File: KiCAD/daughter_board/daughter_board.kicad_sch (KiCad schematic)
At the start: 22 parts, among them IC1 QMC5883L, J1 JST, U1 TPS61023DRLR, U2 SN74AHCT1G125DBVR, U3 XIAO-ESP32-C3-SMD, U4 MPU-6050

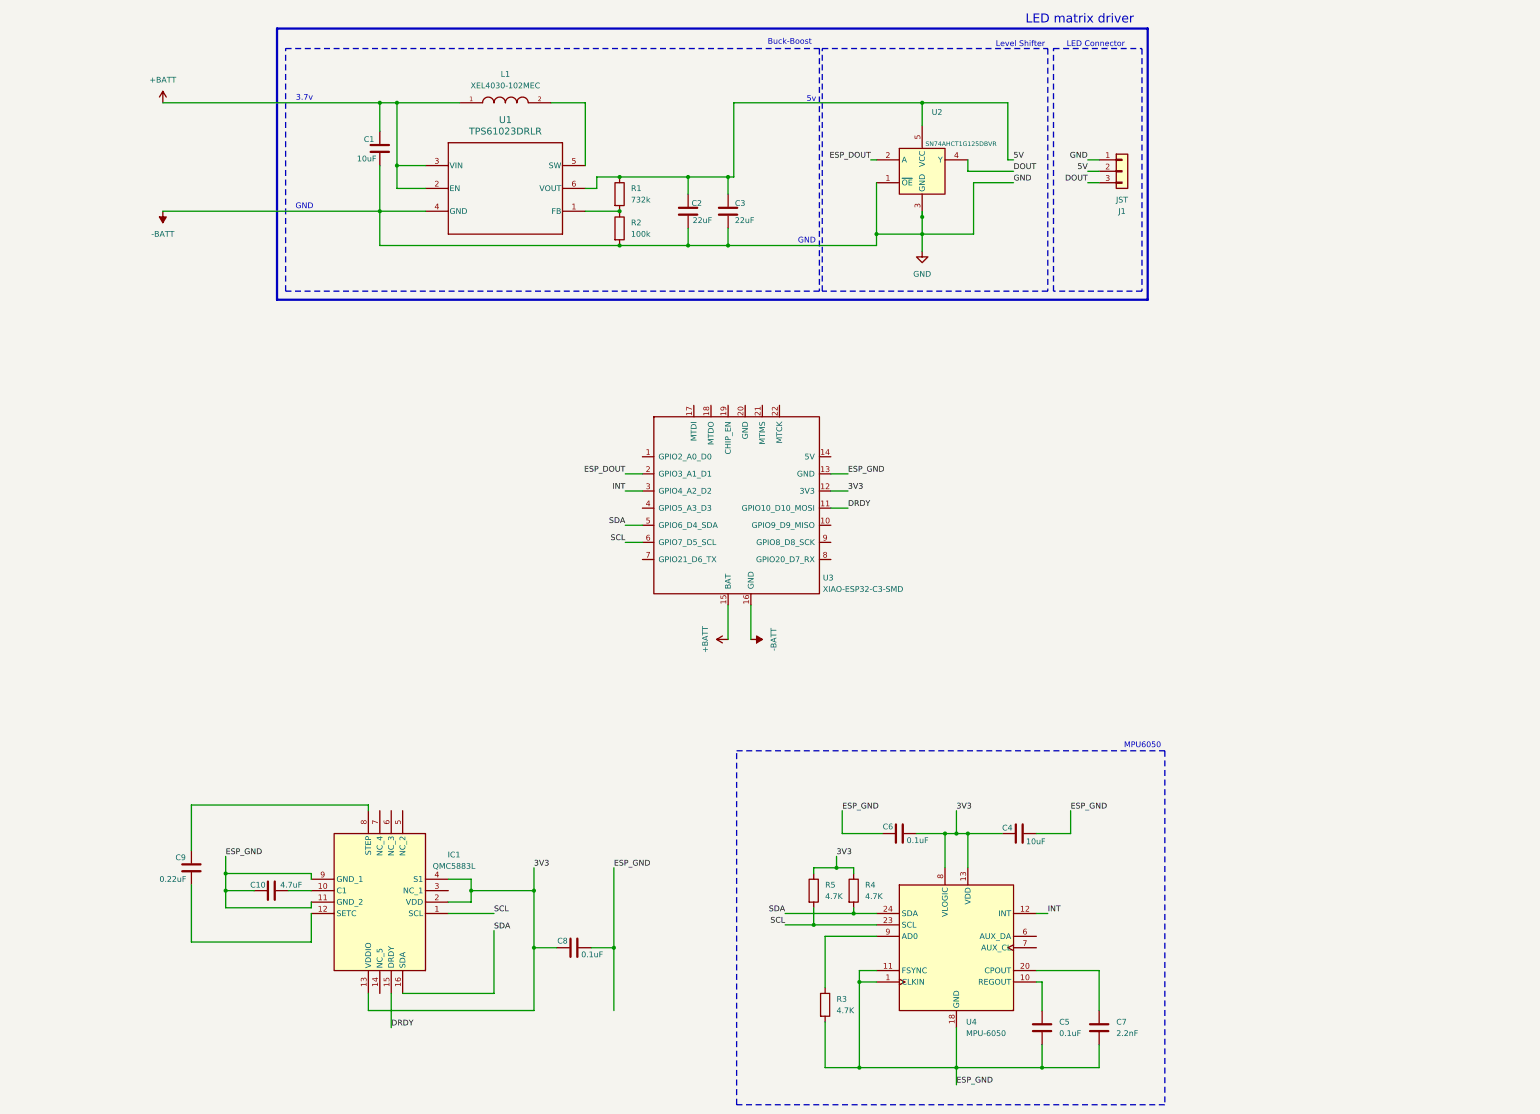
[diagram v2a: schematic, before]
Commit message: kicad schematic finished for the daughter board (initial design)
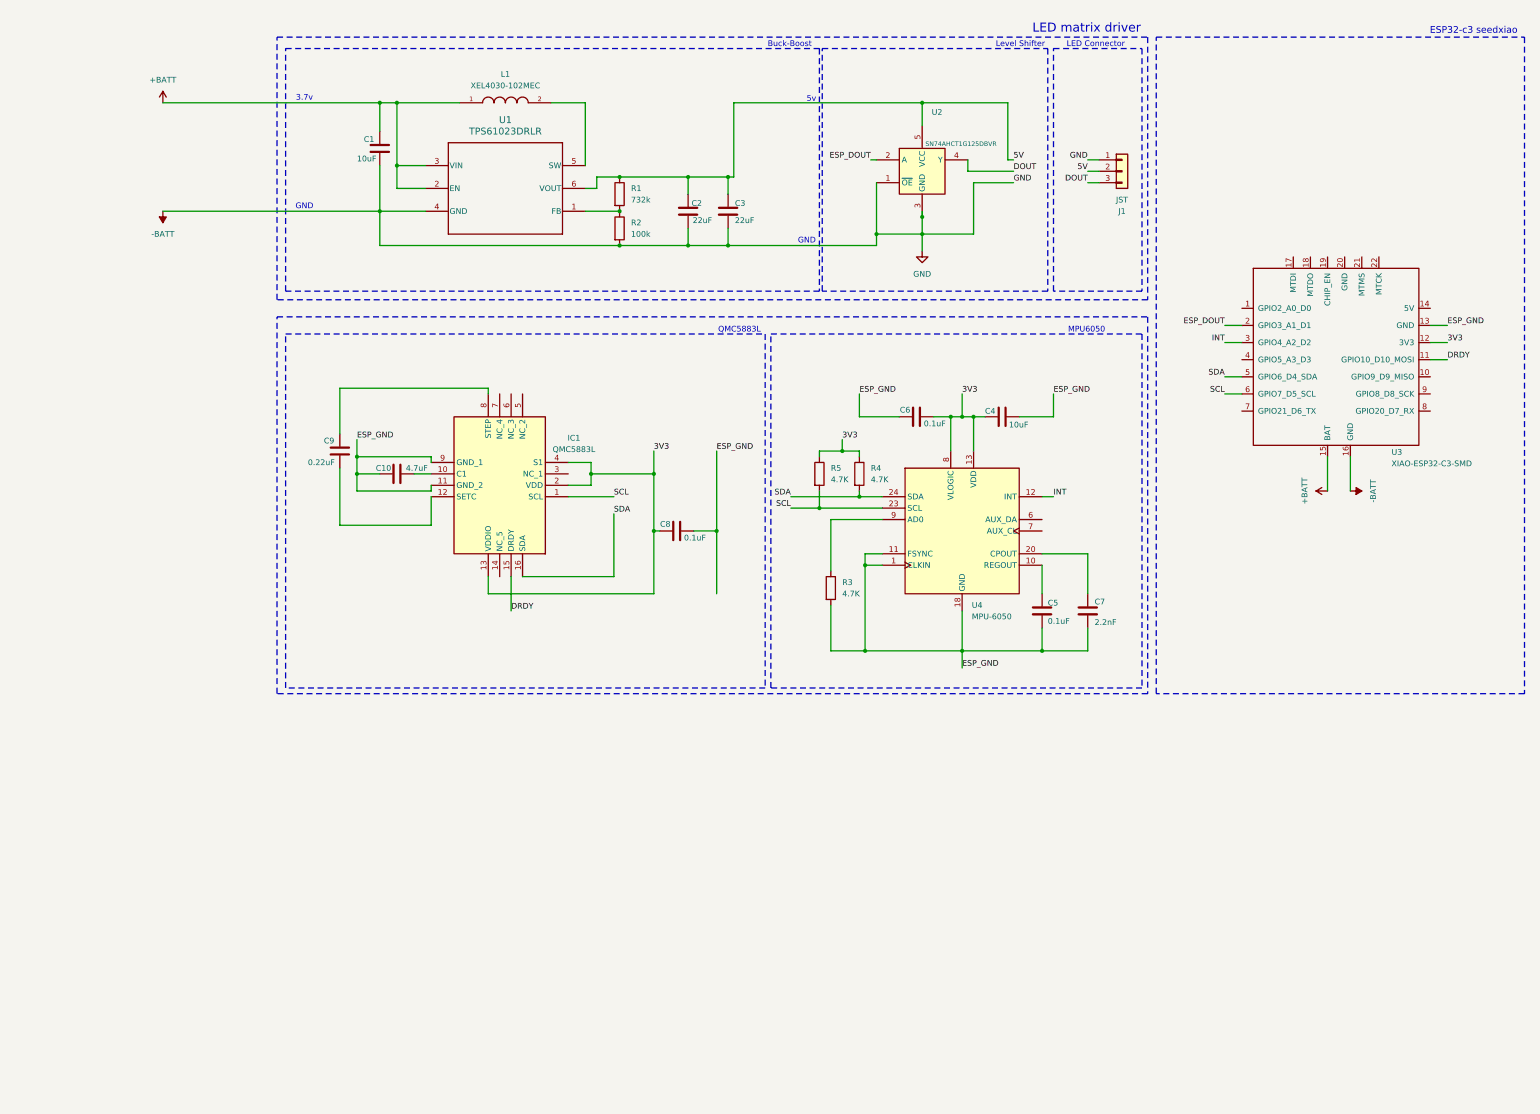
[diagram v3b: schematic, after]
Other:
- note added: "ESP32-c3 seedxiao"
- note added: "QMC5883L"
- moved on the sheet: C10, C4, C5, C6, C7, C8, C9, IC1, R3, R4, R5, U3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

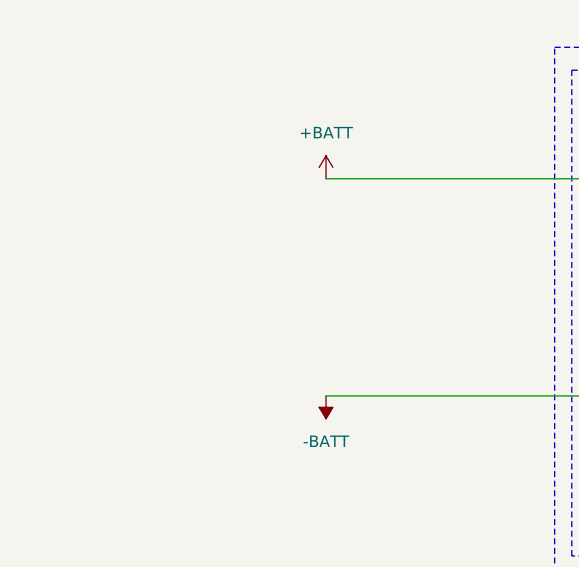
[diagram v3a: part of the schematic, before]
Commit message: added power connector to the schematic, next step is to make the footprint
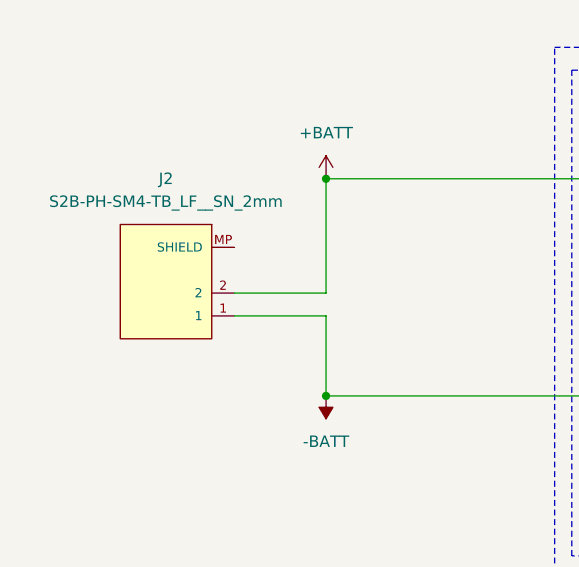
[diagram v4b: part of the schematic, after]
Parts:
- added J2: S2B-PH-SM4-TB_LF__SN_2mm, Connector_JST:JST_PH_S2B-PH-SM4-TB_1x02-1MP_P2.00mm_Horizontal, symbol JST_S2B-PH-SM4-TB_LF__SN_:S2B-PH-SM4-TB_LF__SN_
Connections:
- net +BATT: now also J2.2
- net -BATT: now also J2.1
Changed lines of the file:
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@@
 	)
 	(junction
+		(at 59.69 96.52)
+		(diameter 0)
+		(color 0 0 0 0)
+	)
+	(junction
 		(at 154.94 154.94)
 		(diameter 0)
@@
 	)
 	(junction
+		(at 59.69 72.39)
+		(diameter 0)
+		(color 0 0 0 0)
+	)
+	(junction
 		(at 107.95 72.39)
 		(diameter 0)
@@
 	(wire
 		(pts
+			(xy 49.53 85.09) (xy 59.69 85.09)
+		)
+		(stroke
+			(width 0)
+			(type default)
+		)
+	)
+	(wire
+		(pts
 			(xy 210.82 147.32) (xy 210.82 149.86)
 		)
@@
 	(wire
 		(pts
+			(xy 59.69 85.09) (xy 59.69 72.39)
+		)
+		(stroke
+			(width 0)
+			(type default)
+		)
+	)
+	(wire
+		(pts
 			(xy 240.03 142.24) (xy 240.03 149.86)
 		)
@@
 	(wire
 		(pts
+			(xy 59.69 87.63) (xy 59.69 96.52)
+		)
+		(stroke
+			(width 0)
+			(type default)
+		)
+	)
+	(wire
+		(pts
 			(xy 214.63 142.24) (xy 223.52 142.24)
 		)
@@
 	(wire
 		(pts
+			(xy 49.53 87.63) (xy 59.69 87.63)
+		)
+		(stroke
+			(width 0)
+			(type default)
+		)
+	)
+	(wire
+		(pts
 			(xy 176.53 104.14) (xy 176.53 100.33)
 		)
@@
 					(unit 1)
 				)
+			)
+		)
+	)
+	(symbol
+		(lib_id "JST_S2B-PH-SM4-TB_LF__SN_:S2B-PH-SM4-TB_LF__SN_")
+		(at 41.91 85.09 180)
+		(unit 1)
+		(exclude_from_sim no)
+		(in_bom yes)
+		(on_board yes)
+		(dnp no)
+		(fields_autoplaced yes)
+		(property "Reference" "J2"
+			(at 41.91 72.39 0)
+			(effects
+				(font
+					(size 1.27 1.27)
+				)
+			)
+		)
+		(property "Value" "S2B-PH-SM4-TB_LF__SN_2mm"
+			(at 41.91 74.93 0)
+			(effects
+				(font
+					(size 1.27 1.27)
+				)
+			)
+		)
+		(property "Footprint" "Connector_JST:JST_PH_S2B-PH-SM4-TB_1x02-1MP_P2.00mm_Horizontal"
+			(at 41.91 85.09 0)
+			(effects
+				(font
+					(size 1.27 1.27)
+				)
+				(justify bottom)
+				(hide yes)
+			)
+		)
+		(property "Datasheet" ""
+			(at 41.91 85.09 0)
+			(effects
+				(font
+					(size 1.27 1.27)
+				)
+				(hide yes)
+			)
+		)
+		(property "Description" ""
+			(at 41.91 85.09 0)
+			(effects
+				(font
+					(size 1.27 1.27)
+				)
+				(hide yes)
+			)
+		)
+		(property "MF" "JST Sales"
+			(at 41.91 85.09 0)
+			(effects
+				(font
+					(size 1.27 1.27)
+				)
+				(justify bottom)
+				(hide yes)
+			)
+		)
+		(property "Description_1" "Connector Header Surface Mount, Right Angle 2 position 0.079 (2.00mm)"
+			(at 41.91 85.09 0)
+			(effects
+				(font
+					(size 1.27 1.27)
+				)
+				(justify bottom)
+				(hide yes)
+			)
+		)
+		(property "Package" "None"
+			(at 41.91 85.09 0)
+			(effects
+				(font
+					(size 1.27 1.27)
+				)
+				(justify bottom)
+				(hide yes)
+			)
+		)
+		(property "Price" "None"
+			(at 41.91 85.09 0)
+			(effects
+				(font
+					(size 1.27 1.27)
+				)
+				(justify bottom)
+				(hide yes)
+			)
+		)
+		(property "Check_prices" "https://www.snapeda.com/parts/S2B-PH-SM4-TB(LF)(SN)/JST/view-part/?ref=eda"
+			(at 41.91 85.09 0)
+			(effects
+				(font
+					(size 1.27 1.27)
+				)
+				(justify bottom)
+				(hide yes)
+			)
+		)
+		(property "STANDARD" "Manufacturer Recommendation"
+			(at 41.91 85.09 0)
+			(effects
+				(font
+					(size 1.27 1.27)
+				)
+				(justify bottom)
+				(hide yes)
+			)
+		)
+		(property "SnapEDA_Link" "https://www.snapeda.com/parts/S2B-PH-SM4-TB(LF)(SN)/JST/view-part/?ref=snap"
+			(at 41.91 85.09 0)
+			(effects
+				(font
+					(size 1.27 1.27)
+				)
+				(justify bottom)
+				(hide yes)
+			)
+		)
+		(property "MP" "S2B-PH-SM4-TB(LF)(SN)"
+			(at 41.91 85.09 0)
+			(effects
+				(font
+					(size 1.27 1.27)
+				)
+				(justify bottom)
+				(hide yes)
+			)
+		)
+		(property "Availability" "In Stock"
+			(at 41.91 85.09 0)
+			(effects
+				(font
+					(size 1.27 1.27)
+				)
+				(justify bottom)
+				(hide yes)
+			)
+		)
+		(property "MANUFACTURER" "JST"
+			(at 41.91 85.09 0)
+			(effects
+				(font
+					(size 1.27 1.27)
+				)
+				(justify bottom)
+				(hide yes)
+			)
+		)
+		(pin "1"
+		)
+		(pin "2"
+		)
+		(pin "MP"
+		)
+		(pin "MP"
+		)
+		(instances
+			(project ""
+				(path "/d928dfc7-4203-47ba-85a4-5f555cf64e96"
+					(reference "J2")
+					(unit 1)
+				)

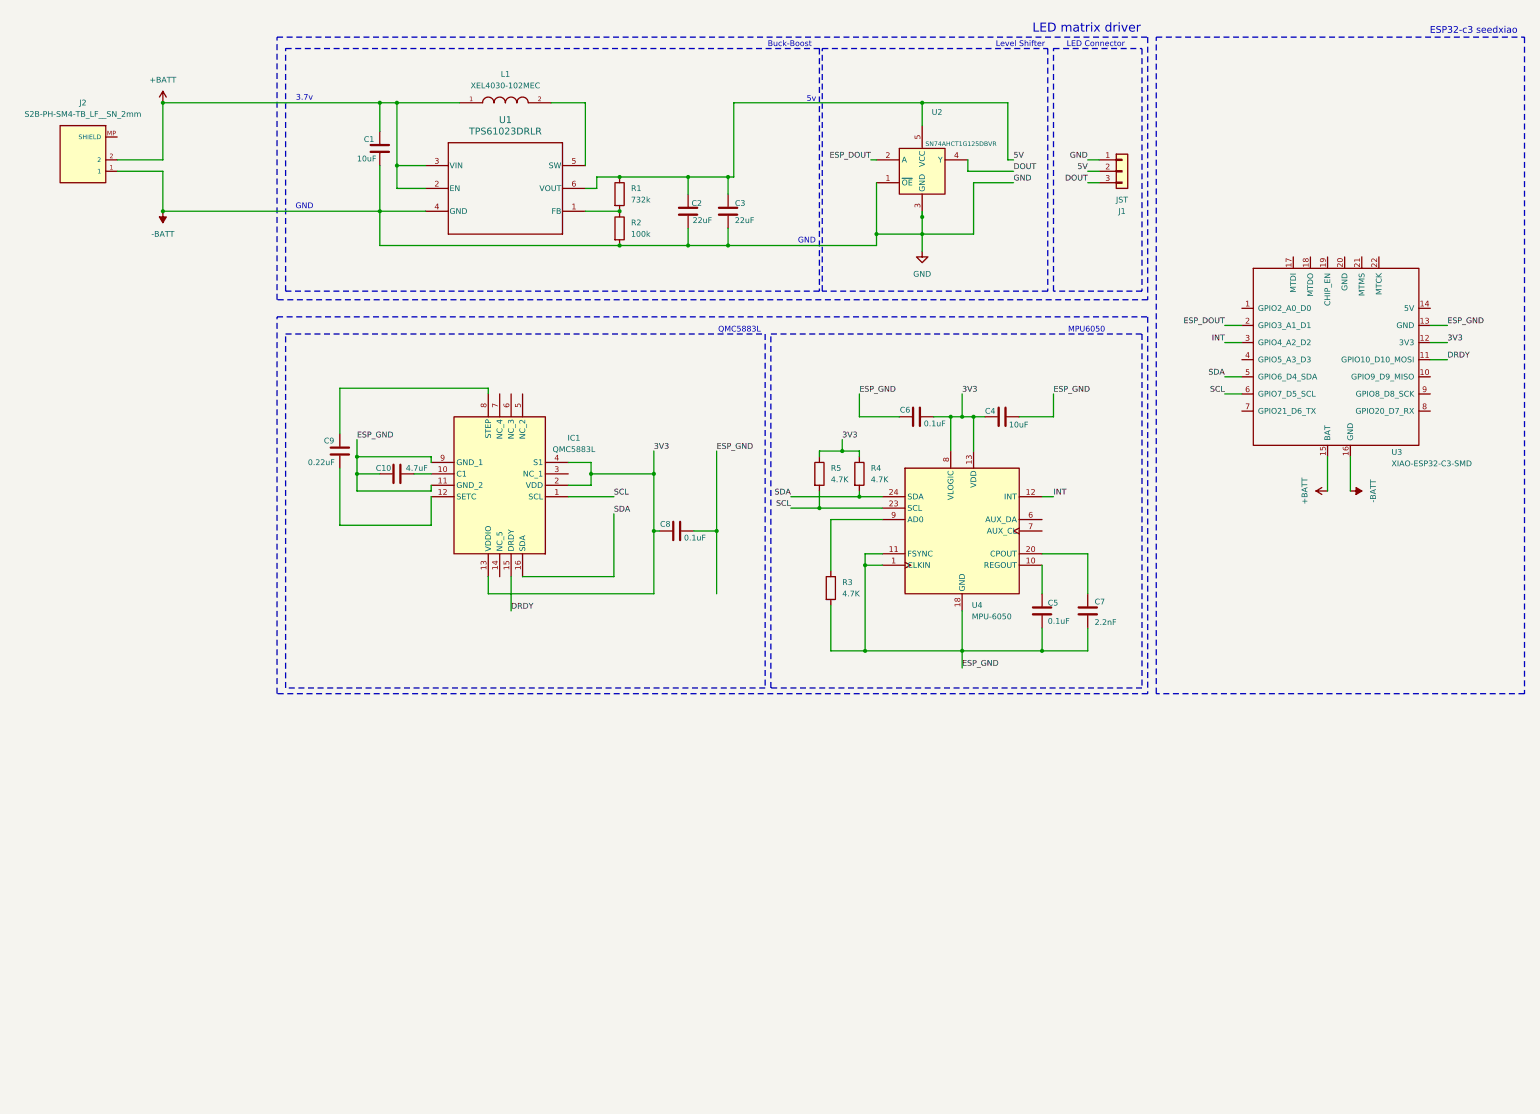
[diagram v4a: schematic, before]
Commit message: completed new freecad base_plate and the KiCAD pcb design
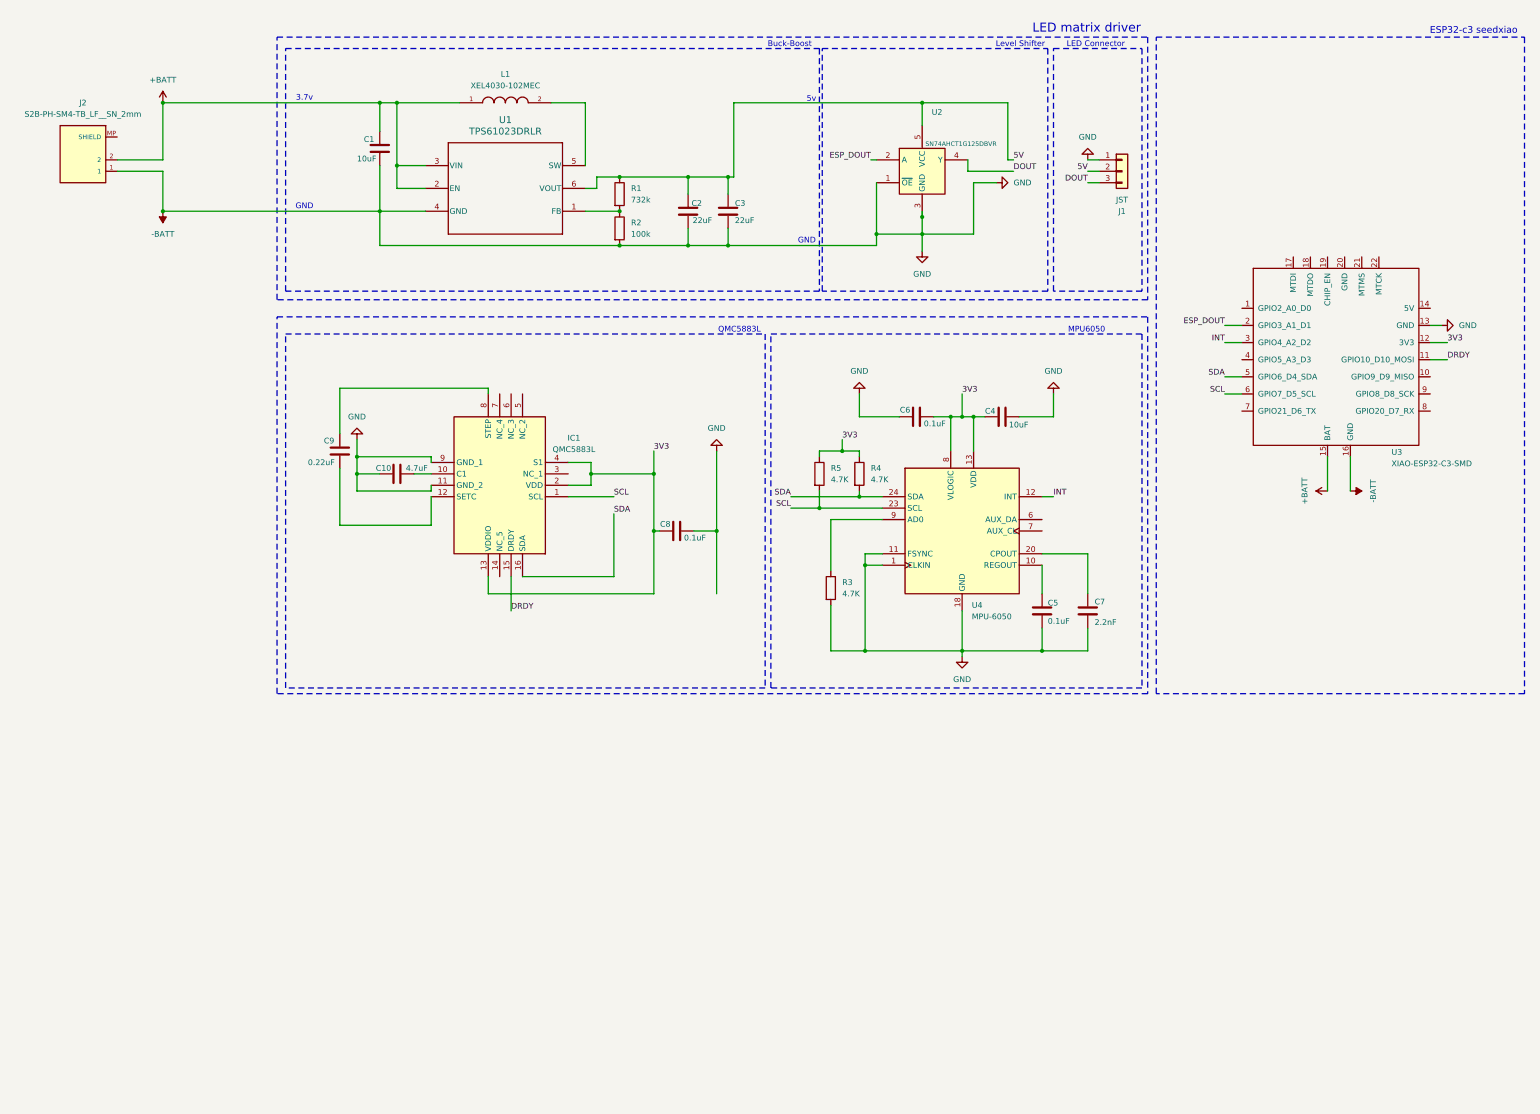
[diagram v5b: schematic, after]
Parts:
- R1, R2: footprint Resistor_SMD:R_0201_0603Metric -> Resistor_SMD:R_0603_1608Metric_Pad0.98x0.95mm_HandSolder
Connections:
- net ESP_GND is gone; now on net -BATT: C10.2, C4.1, C5.2, C6.2, C7.2, C8.1, IC1.11 (GND_2), IC1.9 (GND_1), R3.2, U3.13 (GND), U4.1 (CLKIN), U4.11 (FSYNC), U4.18 (GND)

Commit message: in /FreeCAD model added skrews and the final daughter board,also in /Kicad added voletage divider in daughter board
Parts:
- added R6, R7: 100k, Resistor_SMD:R_0603_1608Metric_Pad0.98x0.95mm_HandSolder, symbol Device:R
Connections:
- net +BATT: now also R7.1
- net -BATT: now also R6.2
- net ADC: now reaches U3.1 (GPIO2_A0_D0)
- net ADC: now also R6.1, R7.2
